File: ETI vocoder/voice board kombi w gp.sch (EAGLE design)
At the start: 174 parts, among them IC1 TL072P, IC1. TL072P, IC2 TL072P, IC2. TL072P, IC3 TL081P, IC3. TL081P, IC4 TL081P, IC4. TL081P, IC5 TL072P, IC6 LM13600AN, IC7 TL072P, IC7. TL072P, P1 C-OR-R050_075-025X100, P1. C-OR-R050_075-025X100, P10 C-OR-R050_075-025X100, P10. C-OR-R050_075-025X100, P11 C-OR-R050_075-025X100, P11. C-OR-R050_075-025X100, P12 C-OR-R050_075-025X100, P12. C-OR-R050_075-025X100, P13 C-OR-R050_075-025X100, P13. C-OR-R050_075-025X100, P14 C-OR-R050_075-025X100, P14. C-OR-R050_075-025X100, P15 C-OR-R050_075-025X100, P15. C-OR-R050_075-025X100, P16 C-OR-R050_075-025X100, P16. C-OR-R050_075-025X100, P2 C-OR-R050_075-025X100, P2. C-OR-R050_075-025X100, P3 C-OR-R050_075-025X100, P3. C-OR-R050_075-025X100, P4 C-OR-R050_075-025X100, P4. C-OR-R050_075-025X100, P5 C-OR-R050_075-025X100, P5. C-OR-R050_075-025X100, P6 C-OR-R050_075-025X100, P6. C-OR-R050_075-025X100, P7 C-OR-R050_075-025X100, P7. C-OR-R050_075-025X100, P8 C-OR-R050_075-025X100, P8. C-OR-R050_075-025X100, P9 C-OR-R050_075-025X100, P9. C-OR-R050_075-025X100, Q1 BF244C, Q1. BF244C, Q2 BC212L, Q2. BC212L

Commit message: Renamed components to better match parts list from the article. Any part that is not consistent across HP/LP/BP now has either CE, RE or P prefix
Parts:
- removed C2, C2.: (no value), joakim:C-EU050_075-025X100
- removed R2, R2., R4, R4.: (no value), resistor:R-US_0207/7
- added CE4, CE4.: (no value), resistor:CPOL-EUE2-4
- added RE6, RE6.: (no value), resistor:R-US_0204/7
- added RE7, RE7.: (no value), resistor:R-US_0207/7
- CE2, CE2.: device resistor:CPOL-EUE2-4 -> joakim:C-EU050_075-025X100
- renumbered C11 to CE6, C11. to CE6., C4 to CE3, C4. to CE3., C9 to CE5, C9. to CE5., R22 to RE8, R22. to RE8., R24 to RE9, R24. to RE9., R25 to RE10, R25. to RE10., R33 to R35, R33. to R35., R34 to R36, R34. to R36., R5 to RE5, R5. to RE5.
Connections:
- net EXCITATION_IN: now also CE4.+, CE4..+; no longer CE2.+, CE2..+
- net GND: now also RE6..1, RE6.1, RE7..1, RE7.1; no longer R4..1, R4.1, RE3..1, RE3.1
- net N$1: now also RE3.1; no longer R2.1
- net N$2: now also CE2.1; no longer C2.1
- net N$29: now also RE7.2; no longer RE3.2
- net N$3: now also CE2.2, RE3.2; no longer C2.2, R2.2
- net N$45: now also CE4.-; no longer CE2.-
- net N$46: now also RE6.2; no longer RE4.2
- net N$47: now also RE3..1; no longer R2..1
- net N$48: now also CE2..1; no longer C2..1
- net N$49: now also CE2..2, RE3..2; no longer C2..2, R2..2
- net N$5: now also RE4.2; no longer R4.2
- net N$50: now also RE4..2; no longer R4..2
- net N$75: now also RE7..2; no longer RE3..2
- net N$90: now also CE4..-; no longer CE2..-
- net N$91: now also RE6..2; no longer RE4..2
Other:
- note added: "B: n/c H: n/c L: R34"
- note added: "P12 eksisterer ikke, fikse?"
- note removed: "B: N/C H: N/C L: R34"
- moved on the sheet: P12, P12., RE3, RE3., RE4, RE4.

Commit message: Separated LP/BP from BP/HP channels (left channel is never HP, right is never LP). Removed unused/shorted parts. Replaced all caps with wider ones w. 5mm pitch (may have to make them even wider). Replaced parts in left/right channel that had P footprints with R or C if they are now only one type combined with either N/C or short.
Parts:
- removed CE1., CE4.: (no value), resistor:CPOL-EUE2-4
- removed RE1.: (no value), resistor:R-US_0207/7
- removed RE6.: (no value), resistor:R-US_0204/7
- C12, C12., C5, C5., C6, C6., C7, C7., CE2, CE2., CE3, CE3., CE5, CE5., CE6, CE6.: device joakim:C-EU050_075-025X100 -> resistor:C-EU050-030X075
- P1, P11, P12., P13, P15, P16., P3, P4., P5, P7, P8., P9: value C-OR-R050_075-025X100 -> (none); device joakim:C-OR-R050_075-025X100 -> resistor:R-US_0207/7
- P10, P11., P12, P14, P15., P2, P3., P4, P6, P7.: value C-OR-R050_075-025X100 -> (none); device joakim:C-OR-R050_075-025X100 -> resistor:C-EU050-030X075
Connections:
- removed net N$88: CE1..-, P1..2, RE1..2
- removed net N$90: CE4..-, P9..1
- net EXCITATION_IN: now also P9..1; no longer CE4..+
- net GND: no longer RE1..1, RE6..1
- net N$91: no longer RE6..2
- net SPEECH_IN: now also P1..2; no longer CE1..+
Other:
- note added: "B: C1 H: R1"
- note added: "B: C10 H: R26"
- note added: "B: C11 H: N/C"
- note added: "B: C2 H: N/C"
- note added: "B: C3 H: R6"
- note added: "B: C4 H: N/C"
- note added: "B: C8 H: R21"
- note added: "B: C9 H: N/C"
- note added: "B: N/C H: C11"
- note added: "B: N/C H: C2"
- note added: "B: N/C H: C4"
- note added: "B: N/C H: C9"
- note added: "B: N/C H: R24"
- note added: "B: N/C H: R4"
- note added: "B: PR1 H: N/C"
- note added: "B: PR5 H: N/C"
- note added: "B: R1 H: C1"
- note added: "B: R2 H: R3"
- note added: "B: R21 H: C8"
- note added: "B: R22 H: R23"
- note added: "B: R23 H: C10"
- note added: "B: R24 H: N/C"
- note added: "B: R25 H: short"
- note added: "B: R26 H: R25"
- note added: "B: R3 H: C3"
- note added: "B: R4 H: N/C"
- note added: "B: R5 H: short"
- note added: "B: R6 H: R5"
- note added: "B: short H: R2"
- note added: "B: short H: R22"
- note added: "CH 14: HP"
- note added: "CH1: LP"
- note added: "L: C1 B: short"
- note added: "L: C10 B: R26"
- note added: "L: C11 B: C10"
- note added: "L: C13 B: short"
- note added: "L: C14 B: short"
- note added: "L: C2 B: C1"
- note added: "L: C3 B: R6"
- note added: "L: C4 B: C3"
- note added: "L: C8 B: short"
- note added: "L: C9 B: C8"
- note added: "L: N/C B: C11"
- note added: "L: N/C B: C2"
- note added: "L: N/C B: C4"
- note added: "L: N/C B: C9"
- note added: "L: N/C B: PR1"
- note added: "L: N/C B: PR5"
- note added: "L: N/C B: R24"
- note added: "L: N/C B: R4"
- note added: "L: R1 B: R1"
- note added: "L: R2 B: N/C"
- note added: "L: R21 B: R21"
- note added: "L: R22 B: N/C"
- note added: "L: R23 B: R22"
- note added: "L: R24 B: N/C"
- note added: "L: R25 B: R23"
- note added: "L: R26 B: N/C"
- note added: "L: R3 B: R2"
- note added: "L: R33 B: N/C"
- note added: "L: R34 B: n/c"
- note added: "L: R4 B: N/C"
- note added: "L: R5 B: R3"
- note added: "L: R6 B: N/C"
- note added: "L: short B: R25"
- note added: "L: short B: R5"
- note added: "TODO: ALLE CAPS: SJEKKE BREDDE! OG CLEARANCE TIL IC-SOKLER"
- note removed: "B: C1 H: R1 L: C2"
- note removed: "B: C10 H: R26 L: C11"
- note removed: "B: C11 H: N/C L: N/C"
- note removed: "B: C2 H: N/C L: N/C"
- note removed: "B: C3 H: R6 L: C4"
- note removed: "B: C4 H: N/C L: N/C"
- note removed: "B: C8 H: R21 L: C9"
- note removed: "B: C9 H: N/C L: N/C"
- note removed: "B: N/C H: C11 L: R26"
- note removed: "B: N/C H: C2 L: R2"
- note removed: "B: N/C H: C4 L: R6"
- note removed: "B: N/C H: C9 L: R22"
- note removed: "B: N/C H: N/C L: R33"
- note removed: "B: N/C H: R24 L: R24"
- note removed: "B: N/C H: R4 L: R4"
- note removed: "B: PR1 H: N/C L: N/C"
- note removed: "B: PR5 H: N/C L: N/C"
- note removed: "B: R1 H: C1 L: R1"
- note removed: "B: R2 H: R3 L: R3"
- note removed: "B: R21 H: C8 L: R21"
- note removed: "B: R22 H: R23 L: R23"
- note removed: "B: R23 H: C10 L: R25"
- note removed: "B: R24 H: N/C L: N/C"
- note removed: "B: R25 H: short L: short"
- note removed: "B: R26 H: R25 L: C10"
- note removed: "B: R3 H: C3 L: R5"
- note removed: "B: R4 H: N/C L: N/C"
- note removed: "B: R5 H: short L: short"
- note removed: "B: R6 H: R5 L: C3"
- note removed: "B: n/c H: n/c L: R34"
- note removed: "B: short H: R2 L: C1"
- note removed: "B: short H: R22 L: C8"
- note removed: "B: short H: short L: C13"
- note removed: "B: short H: short L: C14"

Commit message: Changed all caps and C-or-Rs for 5mm pitch 3mm wide ones
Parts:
- P1., P10., P13., P14., P16, P2., P5., P6., P8, P9.: value C-OR-R050_075-025X100 -> C-OR-R050_075-030X100; device joakim:C-OR-R050_075-025X100 -> joakim:C-OR-R050_075-030X100
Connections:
- new net N$88: P15..1, RE9..2
- net N$74: now also P13..1; no longer P13..2, P15..1, RE9..2
- net N$76: now also P13..2; no longer P13..1
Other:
- moved on the sheet: P13.
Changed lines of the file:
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@@
 <part name="P4" library="resistor" deviceset="C-EU" device="050-030X075"/>
 <part name="RE6" library="resistor" deviceset="R-US_" device="0204/7"/>
-<part name="P8" library="joakim" deviceset="C-OR-R" device="050_075-025X100"/>
-<part name="P16" library="joakim" deviceset="C-OR-R" device="050_075-025X100"/>
+<part name="P8" library="joakim" deviceset="C-OR-R" device="050_075-030X100" value="C-OR-R050_075-030X100"/>
+<part name="P16" library="joakim" deviceset="C-OR-R" device="050_075-030X100" value="C-OR-R050_075-030X100"/>
 <part name="RV1" library="joakim" deviceset="POT16_W_BRACKET" device="&quot;&quot;" value="100k log"/>
 <part name="P+5" library="supply1" deviceset="+12V" device=""/>
@@
 <part name="GND21" library="supply1" deviceset="GND" device=""/>
 <part name="IC1." library="linear" deviceset="TL072" device="P"/>
-<part name="P1." library="joakim" deviceset="C-OR-R" device="050_075-025X100"/>
+<part name="P1." library="joakim" deviceset="C-OR-R" device="050_075-030X100" value="C-OR-R050_075-030X100"/>
 <part name="RE3." library="resistor" deviceset="R-US_" device="0207/7"/>
-<part name="P5." library="joakim" deviceset="C-OR-R" device="050_075-025X100"/>
+<part name="P5." library="joakim" deviceset="C-OR-R" device="050_075-030X100" value="C-OR-R050_075-030X100"/>
 <part name="RE4." library="resistor" deviceset="R-US_" device="0207/7"/>
 <part name="RE5." library="resistor" deviceset="R-US_" device="0207/7"/>
@@
 <part name="R9." library="resistor" deviceset="R-US_" device="0207/7"/>
 <part name="PR1." library="pot" deviceset="TRIM_EU-" device="CA9V"/>
-<part name="P2." library="joakim" deviceset="C-OR-R" device="050_075-025X100"/>
+<part name="P2." library="joakim" deviceset="C-OR-R" device="050_075-030X100" value="C-OR-R050_075-030X100"/>
 <part name="CE2." library="resistor" deviceset="C-EU" device="050-030X075"/>
-<part name="P6." library="joakim" deviceset="C-OR-R" device="050_075-025X100"/>
+<part name="P6." library="joakim" deviceset="C-OR-R" device="050_075-030X100" value="C-OR-R050_075-030X100"/>
 <part name="CE3." library="resistor" deviceset="C-EU" device="050-030X075"/>
 <part name="GND23" library="supply1" deviceset="GND" device=""/>
@@
 <part name="GND30" library="supply1" deviceset="GND" device=""/>
 <part name="R20." library="resistor" deviceset="R-US_" device="0207/7"/>
-<part name="P9." library="joakim" deviceset="C-OR-R" device="050_075-025X100"/>
+<part name="P9." library="joakim" deviceset="C-OR-R" device="050_075-030X100" value="C-OR-R050_075-030X100"/>
 <part name="RE8." library="resistor" deviceset="R-US_" device="0207/7"/>
-<part name="P13." library="joakim" deviceset="C-OR-R" device="050_075-025X100"/>
+<part name="P13." library="joakim" deviceset="C-OR-R" device="050_075-030X100" value="C-OR-R050_075-030X100"/>
 <part name="RE9." library="resistor" deviceset="R-US_" device="0207/7"/>
 <part name="RE10." library="resistor" deviceset="R-US_" device="0207/7"/>
@@
 <part name="PR4." library="pot" deviceset="TRIM_EU-" device="CA9V"/>
 <part name="PR5." library="pot" deviceset="TRIM_EU-" device="CA9V"/>
-<part name="P10." library="joakim" deviceset="C-OR-R" device="050_075-025X100"/>
+<part name="P10." library="joakim" deviceset="C-OR-R" device="050_075-030X100" value="C-OR-R050_075-030X100"/>
 <part name="CE5." library="resistor" deviceset="C-EU" device="050-030X075"/>
-<part name="P14." library="joakim" deviceset="C-OR-R" device="050_075-025X100"/>
+<part name="P14." library="joakim" deviceset="C-OR-R" device="050_075-030X100" value="C-OR-R050_075-030X100"/>
 <part name="CE6." library="resistor" deviceset="C-EU" device="050-030X075"/>
 <part name="C12." library="resistor" deviceset="C-EU" device="050-030X075"/>
@@
 <attribute name="VALUE" x="102.87" y="11.938" size="1.778" layer="96"/>
 </instance>
-<instance part="P13." gate="G$1" x="121.92" y="0" smashed="yes" rot="R90">
+<instance part="P13." gate="G$1" x="121.92" y="0" smashed="yes" rot="R270">
 <attribute name="NAME" x="118.364" y="8.001" size="1.778" layer="95"/>
 </instance>
@@
 <net name="N$74" class="0">
 <segment>
-<pinref part="P13." gate="G$1" pin="2"/>
 <pinref part="P14." gate="G$1" pin="2"/>
-<pinref part="RE9." gate="G$1" pin="2"/>
 <pinref part="CE6." gate="G$1" pin="2"/>
 <wire x1="142.24" y1="17.78" x2="127" y2="17.78" width="0.1524" layer="91"/>
 <wire x1="127" y1="17.78" x2="127" y2="0" width="0.1524" layer="91"/>
 <wire x1="127" y1="0" x2="129.54" y2="0" width="0.1524" layer="91"/>
-<wire x1="127" y1="-5.08" x2="127" y2="0" width="0.1524" layer="91"/>
+<pinref part="P13." gate="G$1" pin="1"/>
 <junction x="127" y="0"/>
-<pinref part="P15." gate="G$1" pin="1"/>
-<wire x1="127" y1="-5.08" x2="132.08" y2="-5.08" width="0.1524" layer="91"/>
-<junction x="127" y="-5.08"/>
 </segment>
 </net>
@@
 <net name="N$76" class="0">
 <segment>
-<pinref part="IC7." gate="A" pin="OUT"/>
-<pinref part="P13." gate="G$1" pin="1"/>
 <pinref part="CE5." gate="G$1" pin="1"/>
 <wire x1="106.68" y1="20.32" x2="116.84" y2="20.32" width="0.1524" layer="91"/>
 <wire x1="116.84" y1="20.32" x2="116.84" y2="15.24" width="0.1524" layer="91"/>
 <pinref part="RE8." gate="G$1" pin="2"/>
+<wire x1="111.76" y1="15.24" x2="116.84" y2="15.24" width="0.1524" layer="91"/>
+<pinref part="IC7." gate="A" pin="OUT"/>
+<pinref part="P13." gate="G$1" pin="2"/>
 <wire x1="116.84" y1="15.24" x2="116.84" y2="0" width="0.1524" layer="91"/>
-<wire x1="111.76" y1="15.24" x2="116.84" y2="15.24" width="0.1524" layer="91"/>
-<junction x="116.84" y="15.24"/>
 <junction x="116.84" y="0"/>
 </segment>
@@
 </segment>
 </net>
+<net name="N$88" class="0">
+<segment>
+<pinref part="P15." gate="G$1" pin="1"/>
+<pinref part="RE9." gate="G$1" pin="2"/>
+<wire x1="127" y1="-5.08" x2="132.08" y2="-5.08" width="0.1524" layer="91"/>
+</segment>
+</net>

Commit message: Finished capacitor spacing tweaks, ic sockets should fit now
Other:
- note added: "Naming: P: Part - C, R, N/C or Short CE: Capacitor that has different number on different channels RE: Resistor that has different number on different channels See B/H/L for article part numbers The rest has the same names as in the article."
- note removed: "CH 14: HP"
- note removed: "CH1: LP"
- note removed: "Naming: P: Part - C, R, N/C or Short CE: Extra capacitor not on BP RE: Extra resistor not on BP See B/H/L for article part numbers The rest has the same names as in the article."
- note removed: "P12 eksisterer ikke, fikse?"
- note removed: "TODO: ALLE CAPS: SJEKKE BREDDE! OG CLEARANCE TIL IC-SOKLER"
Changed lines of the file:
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@@
 <text x="180.34" y="175.26" size="1.778" layer="97">Error in parts list,
 should be BF244C</text>
-<text x="-33.02" y="246.38" size="1.778" layer="97">Naming:
+<text x="-71.12" y="238.76" size="1.778" layer="97">Naming:
 P: Part - C, R, N/C or Short
-CE: Extra capacitor not on BP
-RE: Extra resistor not on BP
+CE: Capacitor that has different number on different channels
+RE: Resistor that has different number on different channels
 See B/H/L for article part numbers
 The rest has the same names
@@
 <text x="162.56" y="251.46" size="1.778" layer="97">Do not connect vu detector
 between channel 12 and 13</text>
-<text x="83.82" y="-30.48" size="1.778" layer="91">P12 eksisterer ikke, fikse?</text>
-<text x="-71.12" y="104.14" size="5.08" layer="91">TODO: ALLE CAPS: SJEKKE BREDDE!
-OG CLEARANCE TIL IC-SOKLER</text>
-<text x="-30.48" y="226.06" size="5.08" layer="91">CH1: LP</text>
-<text x="-20.32" y="15.24" size="5.08" layer="91">CH 14: HP</text>
 <text x="60.96" y="141.732" size="1.016" layer="97">L: C14
 B: short
@@
 <wire x1="116.84" y1="15.24" x2="116.84" y2="0" width="0.1524" layer="91"/>
 <junction x="116.84" y="0"/>
-</segment>
-</net>
+<junction x="116.84" y="15.24"/>
+</segment>
+</net>

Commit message: Centered capacitors on resistors for a (hopefully) more tidy look
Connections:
- net N$47: now also P2..1; no longer P2..2
- net N$48: now also P2..2; no longer P2..1
- net N$73: now also P10..1; no longer P10..2
- net N$75: now also P10..2; no longer P10..1
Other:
- moved on the sheet: P10., P2.
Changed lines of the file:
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@@
 <attribute name="VALUE" x="24.13" y="62.23" size="1.778" layer="96" rot="R270"/>
 </instance>
-<instance part="P2." gate="G$1" x="27.94" y="68.58" smashed="yes" rot="R90">
+<instance part="P2." gate="G$1" x="27.94" y="68.58" smashed="yes" rot="R270">
 <attribute name="NAME" x="21.336" y="74.041" size="1.778" layer="95"/>
 </instance>
@@
 <attribute name="VALUE" x="80.01" y="-3.81" size="1.778" layer="96" rot="R270"/>
 </instance>
-<instance part="P10." gate="G$1" x="83.82" y="2.54" smashed="yes" rot="R270">
-<attribute name="NAME" x="81.534" y="9.271" size="1.778" layer="95"/>
+<instance part="P10." gate="G$1" x="83.82" y="2.54" smashed="yes" rot="R90">
+<attribute name="NAME" x="78.994" y="9.271" size="1.778" layer="95"/>
 </instance>
 <instance part="CE5." gate="G$1" x="104.14" y="20.32" smashed="yes" rot="R270">
@@
 <segment>
 <pinref part="IC1." gate="A" pin="-IN"/>
-<pinref part="P2." gate="G$1" pin="2"/>
 <pinref part="RE3." gate="G$1" pin="1"/>
-<wire x1="33.02" y1="68.58" x2="35.56" y2="68.58" width="0.1524" layer="91"/>
 <pinref part="RE2." gate="G$1" pin="2"/>
 <wire x1="35.56" y1="81.28" x2="35.56" y2="68.58" width="0.1524" layer="91"/>
+<junction x="35.56" y="81.28"/>
+<pinref part="P2." gate="G$1" pin="1"/>
+<wire x1="33.02" y1="68.58" x2="35.56" y2="68.58" width="0.1524" layer="91"/>
 <junction x="35.56" y="68.58"/>
-<junction x="35.56" y="81.28"/>
 </segment>
 </net>
 <net name="N$48" class="0">
 <segment>
-<pinref part="P2." gate="G$1" pin="1"/>
 <wire x1="20.32" y1="68.58" x2="20.32" y2="86.36" width="0.1524" layer="91"/>
 <pinref part="CE2." gate="G$1" pin="1"/>
@@
 <wire x1="25.4" y1="63.5" x2="20.32" y2="63.5" width="0.1524" layer="91"/>
 <junction x="20.32" y="63.5"/>
-<wire x1="22.86" y1="68.58" x2="20.32" y2="68.58" width="0.1524" layer="91"/>
 <pinref part="P1." gate="G$1" pin="1"/>
 <junction x="20.32" y="68.58"/>
+<pinref part="P2." gate="G$1" pin="2"/>
+<wire x1="22.86" y1="68.58" x2="20.32" y2="68.58" width="0.1524" layer="91"/>
 </segment>
 </net>
@@
 <pinref part="PR5." gate="1" pin="A"/>
 <wire x1="76.2" y1="-2.54" x2="76.2" y2="2.54" width="0.1524" layer="91"/>
-<pinref part="P10." gate="G$1" pin="2"/>
 <wire x1="76.2" y1="2.54" x2="76.2" y2="20.32" width="0.1524" layer="91"/>
 <pinref part="CE5." gate="G$1" pin="2"/>
 <wire x1="76.2" y1="20.32" x2="99.06" y2="20.32" width="0.1524" layer="91"/>
-<wire x1="78.74" y1="2.54" x2="76.2" y2="2.54" width="0.1524" layer="91"/>
 <junction x="76.2" y="2.54"/>
 <junction x="76.2" y="-2.54"/>
 <pinref part="P11." gate="G$1" pin="1"/>
 <wire x1="76.2" y1="-2.54" x2="81.28" y2="-2.54" width="0.1524" layer="91"/>
+<pinref part="P10." gate="G$1" pin="1"/>
+<wire x1="76.2" y1="2.54" x2="78.74" y2="2.54" width="0.1524" layer="91"/>
 </segment>
 </net>
@@
 <net name="N$75" class="0">
 <segment>
-<pinref part="P10." gate="G$1" pin="1"/>
 <pinref part="IC7." gate="A" pin="-IN"/>
 <pinref part="RE8." gate="G$1" pin="1"/>
 <wire x1="101.6" y1="15.24" x2="101.6" y2="2.54" width="0.1524" layer="91"/>
+<pinref part="RE7." gate="G$1" pin="2"/>
+<junction x="101.6" y="15.24"/>
+<pinref part="P10." gate="G$1" pin="2"/>
 <wire x1="88.9" y1="2.54" x2="101.6" y2="2.54" width="0.1524" layer="91"/>
 <junction x="101.6" y="2.54"/>
-<pinref part="RE7." gate="G$1" pin="2"/>
-<junction x="101.6" y="15.24"/>
-</segment>
-</net>
+</segment>
+</net>

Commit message: Various updates while working on the real vocoder
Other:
- note added: "TODO: Replace BF244 with BF245!"
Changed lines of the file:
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@@
 <text x="89.154" y="130.81" size="1.016" layer="97" rot="R180">L: R22
 B: N/C</text>
+<text x="231.14" y="213.36" size="3.81" layer="91">TODO: Replace BF244 with BF245!</text>
 </plain>
 <instances>

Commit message: Added four-legged transistor footprint to allow various JFETs. Changed all caps to 3.5mm wide
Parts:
- C12, C12., C5, C5., C6, C6., C7, C7., CE2, CE2., CE3, CE3., CE5, CE5., CE6, CE6., P10, P11., P12, P14, P15., P2, P3., P4, P6, P7.: device resistor:C-EU050-030X075 -> resistor:C-EU050-035X075
- P1., P10., P13., P14., P16, P2., P5., P6., P8, P9.: value C-OR-R050_075-030X100 -> C-OR-R050_075-035X100; device joakim:C-OR-R050_075-030X100 -> joakim:C-OR-R050_075-035X100
- PR1, PR1., PR2, PR2., PR3, PR3., PR4, PR4., PR5, PR5.: device pot:TRIM_EU-CA9V -> joakim:TRIM_EU-PT10-R065
- Q1, Q1.: device transistor-fet:TN0602N3 -> joakim:N-CHANNEL-JFET-JIL-DGSD
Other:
- moved on the sheet: PR1, PR1., PR2, PR2., PR3, PR3., PR4, PR4., PR5, PR5.

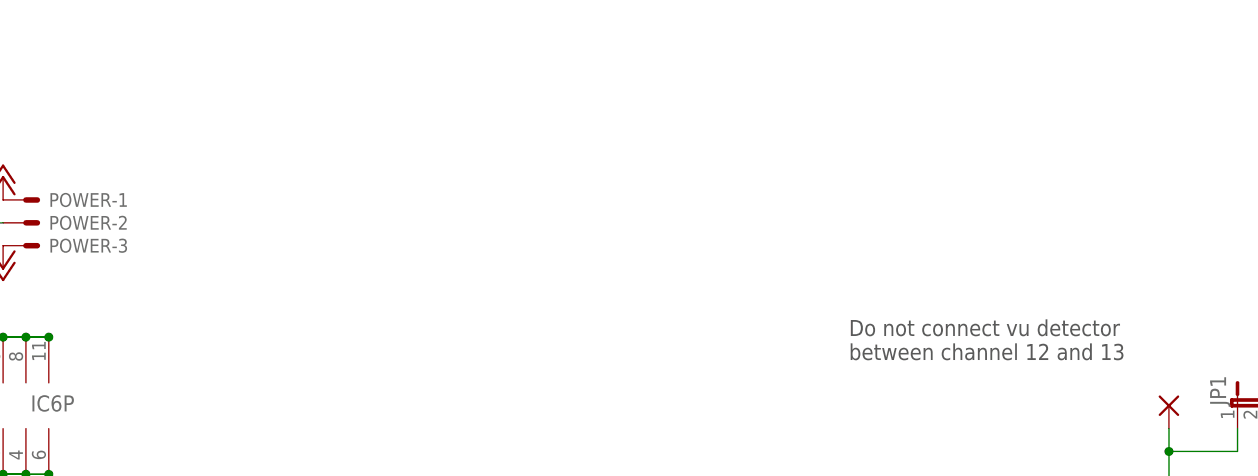
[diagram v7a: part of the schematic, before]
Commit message: Added optional decoupling capacitors. Still need to route and readd groundplanes
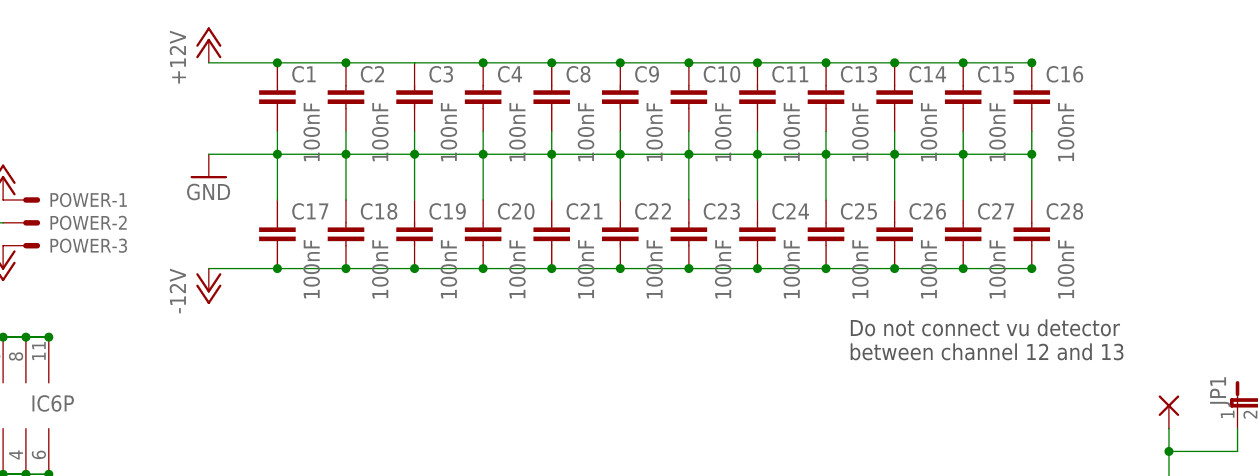
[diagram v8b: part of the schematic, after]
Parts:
- added C1, C10, C11, C13, C14, C15, C16, C17, C18, C19, C2, C20, C21, C22, C23, C24, C25, C26, C27, C28, C3, C4, C8, C9: 100nF, resistor:C-EUC0603
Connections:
- net +12V: now also C1.1, C10.1, C11.1, C13.1, C14.1, C15.1, C16.1, C2.1, C3.1, C4.1, C8.1, C9.1
- net -12V: now also C17.2, C18.2, C19.2, C20.2, C21.2, C22.2, C23.2, C24.2, C25.2, C26.2, C27.2, C28.2
- net GND: now also C1.2, C10.2, C11.2, C13.2, C14.2, C15.2, C16.2, C17.1, C18.1, C19.1, C2.2, C20.1, C21.1, C22.1, C23.1, C24.1, C25.1, C26.1, C27.1, C28.1, C3.2, C4.2, C8.2, C9.2
